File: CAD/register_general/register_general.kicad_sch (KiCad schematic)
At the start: 30 parts, among them J1 Conn_01x16_Pin, J2 Conn_01x16_Pin, U1 74HC245, U2 74HC377

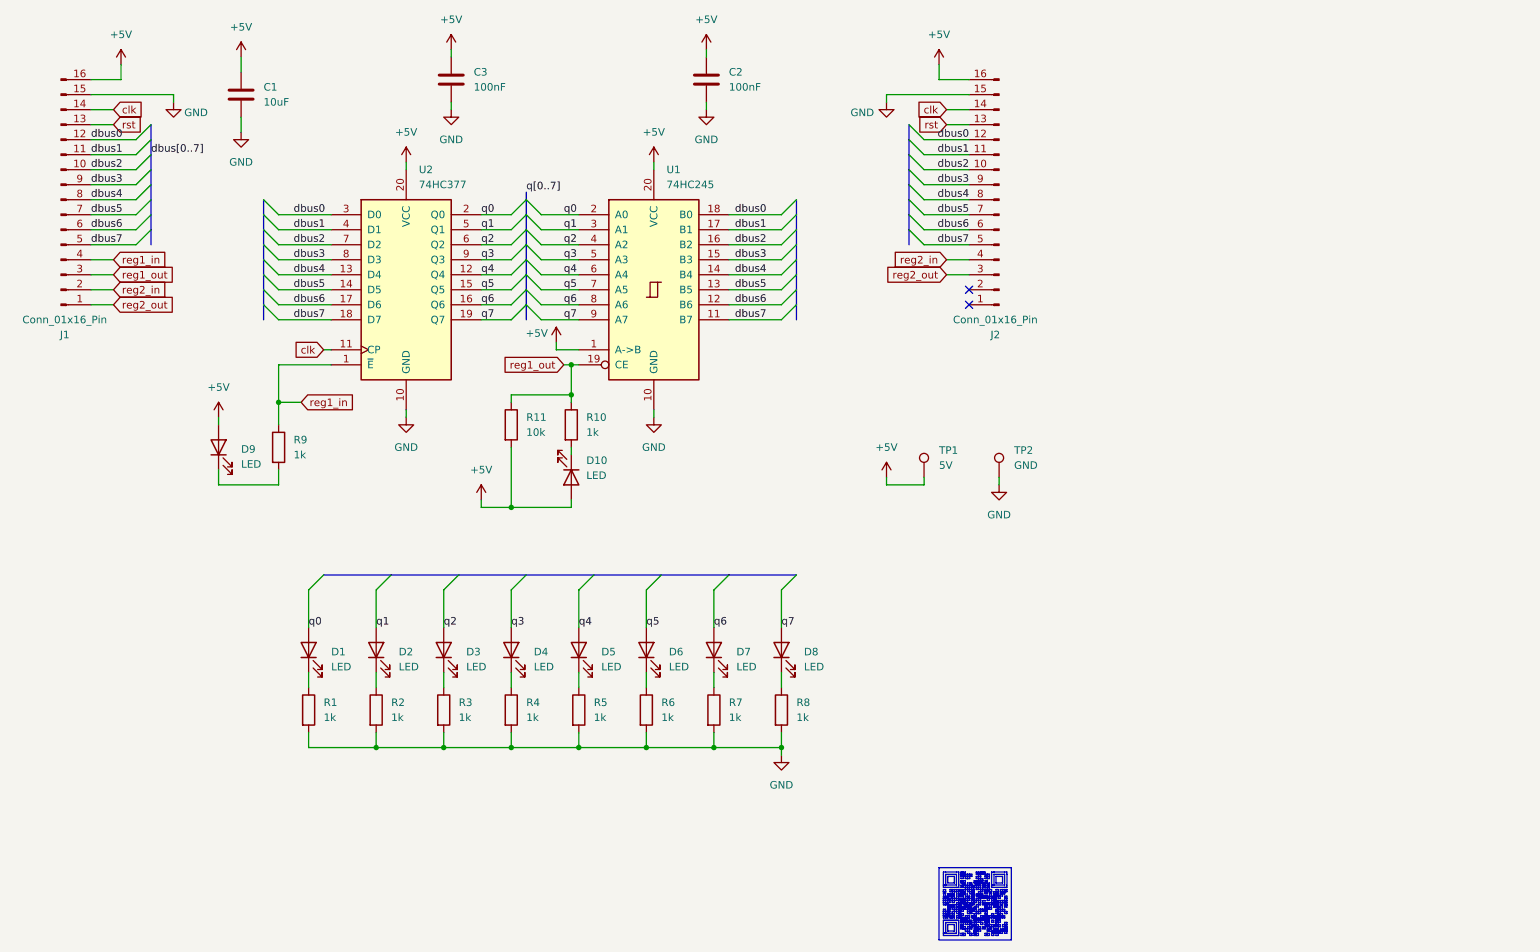
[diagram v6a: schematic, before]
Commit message: update General Register, add mounting holes, testpoints, LCSC numbers
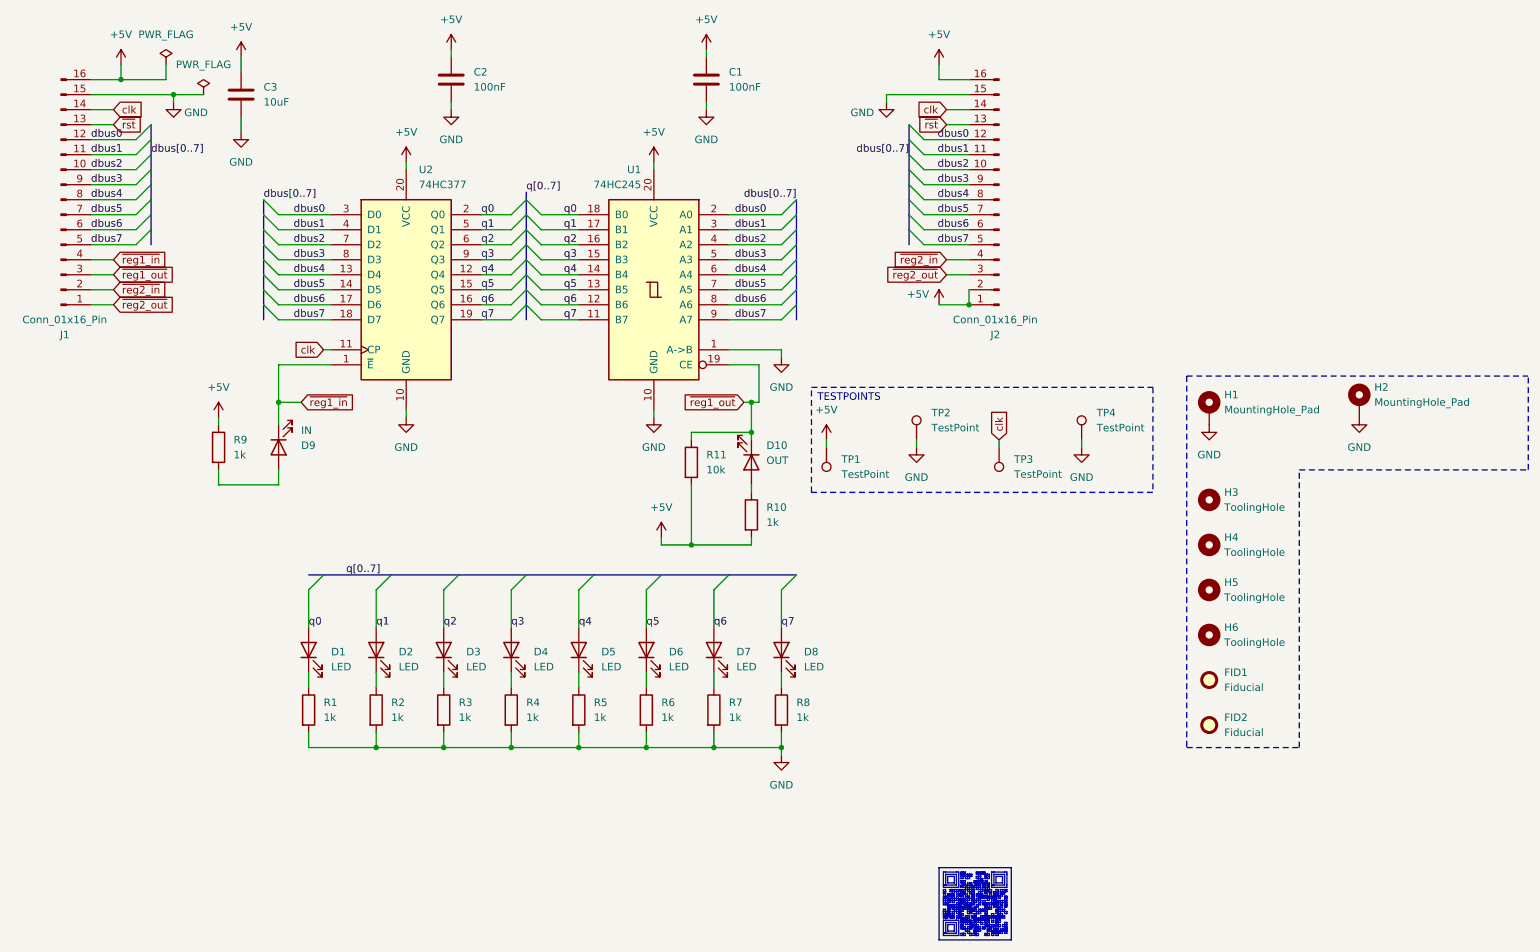
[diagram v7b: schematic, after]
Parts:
- added FID1, FID2: Fiducial, Fiducial:Fiducial_0.5mm_Mask1mm, symbol Mechanical:Fiducial
- added H1, H2: MountingHole_Pad, MountingHole:MountingHole_2.5mm_Pad_Via, symbol Mechanical:MountingHole_Pad
- added H3, H4, H5, H6: ToolingHole, MountingHole:ToolingHole_1.152mm, symbol Mechanical:MountingHole
- added TP3, TP4: TestPoint, TestPoint:TestPoint_THTPad_D1.0mm_Drill0.5mm, symbol Connector:TestPoint
- C1: renamed from C2; LCSC (none) -> C28233
- C2: renamed from C3; LCSC (none) -> C28233
- C3: renamed from C1; LCSC (none) -> C15850
- D1, D2, D3, D4, D5, D6, D7, D8: LCSC (none) -> C84256
- D10: value LED -> OUT; LCSC (none) -> C2296
- D9: value LED -> IN; LCSC (none) -> C2297
- J1: LCSC (none) -> C492436
- J2: LCSC (none) -> C22465965
- R1, R10, R2, R3, R4, R5, R6, R7, R8, R9: LCSC (none) -> C17513
- R11: LCSC (none) -> C17414
- TP1: value 5V -> TestPoint; now left out of the parts list
- TP2: value GND -> TestPoint; now left out of the parts list
- U1: footprint Package_SO:SO-20_5.3x12.6mm_P1.27mm -> Package_SO:SOIC-20W_7.5x12.8mm_P1.27mm; Details https://www.lcsc.com/product-detail/C88578.html -> https://jlcpcb.com/partdetail/Nexperia-74HC245D653/C5625; LCSC C88578 -> C5625
- U2: footprint Package_SO:SO-20_5.3x12.6mm_P1.27mm -> 8-bit_computer:SO-20_5.3x12.6mm_P1.27mm
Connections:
- net +5V: now also J2.1 (Pin_1), J2.2 (Pin_2), R10.2, R9.1; no longer D10.2 (A), D9.2 (A), U1.1 (A->B)
- net GND: now also U1.1 (A->B), H1.1, H2.1, TP4.1
- net clk: now also TP3.1
- net dbus0: now also U1.2 (A0); no longer U1.18 (B0)
- net dbus1: now also U1.3 (A1); no longer U1.17 (B1)
- net dbus2: now also U1.4 (A2); no longer U1.16 (B2)
- net dbus3: now also U1.5 (A3); no longer U1.15 (B3)
- net dbus4: now also U1.6 (A4); no longer U1.14 (B4)
- net dbus5: now also U1.7 (A5); no longer U1.13 (B5)
- net dbus6: now also U1.8 (A6); no longer U1.12 (B6)
- net dbus7: now also U1.9 (A7); no longer U1.11 (B7)
- net q0: now also U1.18 (B0); no longer U1.2 (A0)
- net q1: now also U1.17 (B1); no longer U1.3 (A1)
- net q2: now also U1.16 (B2); no longer U1.4 (A2)
- net q3: now also U1.15 (B3); no longer U1.5 (A3)
- net q4: now also U1.14 (B4); no longer U1.6 (A4)
- net q5: now also U1.13 (B5); no longer U1.7 (A5)
- net q6: now also U1.12 (B6); no longer U1.8 (A6)
- net q7: now also U1.11 (B7); no longer U1.9 (A7)
- net at R9.2: now also D9.2 (A); no longer D9.1 (K)
- net ~{reg1_out}: now reaches D10.1 (K)
- net ~{reg1_out}: now also J1.3 (Pin_3), R11.1, U1.19 (CE); no longer R10.2
- net reg1_in renamed ~{reg1_in}
- net ~{reg1_in}: now also D9.1 (K); no longer R9.1
- removed net reg1_out: J1.3 (Pin_3), R10.1, R11.1, U1.19 (CE)
- net reg2_in renamed ~{reg2_in}
- net reg2_out renamed ~{reg2_out}
- net rst renamed ~{rst}
- new net: D10.2 (A), R10.1
- no-connect marks 2 -> 0
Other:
- note added: "TESTPOINTS"
- moved on the sheet: D10, D9, R10, R11, R9

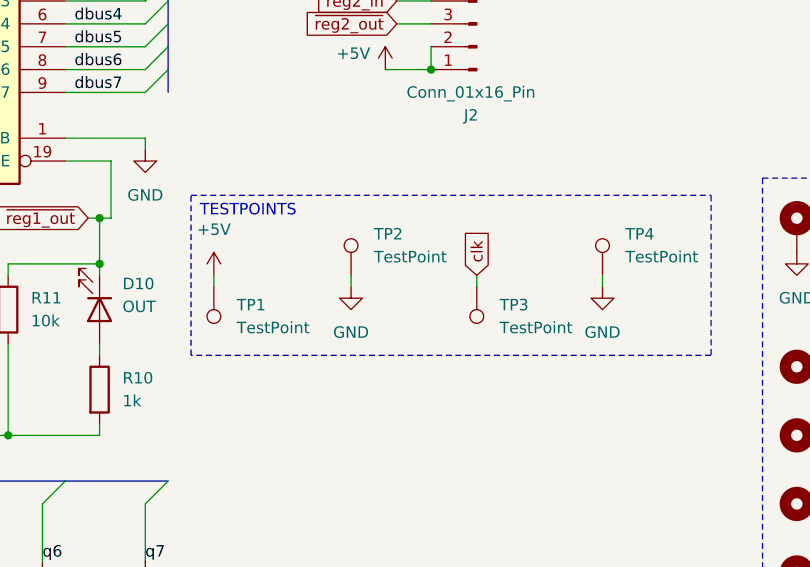
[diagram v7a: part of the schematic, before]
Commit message: add slotted test point for 5V to general register
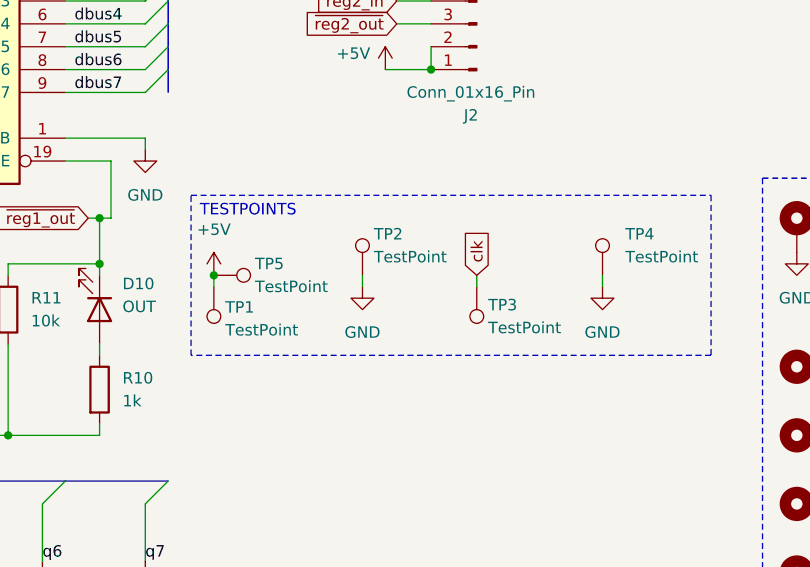
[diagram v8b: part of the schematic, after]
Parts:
- added TP5: TestPoint, 8-bit_computer:TestPoint_Slot_2.2x0.8mm, symbol Connector:TestPoint
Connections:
- net +5V: now also TP5.1
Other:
- moved on the sheet: TP2
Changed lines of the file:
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@@
 	)
 	(junction
+		(at 160.02 95.25)
+		(diameter 0)
+		(color 0 0 0 0)
+	)
+	(junction
 		(at 184.15 72.39)
 		(diameter 0)
@@
 	(wire
 		(pts
-			(xy 175.26 95.25) (xy 175.26 96.52)
+			(xy 176.53 95.25) (xy 176.53 96.52)
 		)
 		(stroke
@@
 		)
 		(instances
-			(project ""
+			(project "register_general"
 				(path "/0d96e788-3788-4603-be87-fd7748d71811"
 					(reference "#PWR03")
@@
 		)
 		(instances
-			(project ""
+			(project "register_general"
 				(path "/0d96e788-3788-4603-be87-fd7748d71811"
 					(reference "#FLG01")
@@
 	(symbol
 		(lib_id "Connector:TestPoint")
-		(at 175.26 95.25 0)
+		(at 176.53 95.25 0)
 		(unit 1)
 		(exclude_from_sim no)
@@
 		(on_board yes)
 		(dnp no)
-		(fields_autoplaced yes)
 		(property "Reference" "TP2"
-			(at 177.8 90.6779 0)
+			(at 177.8 90.678 0)
 			(effects
 				(font
@@
 		)
 		(property "Value" "TestPoint"
-			(at 177.8 93.2179 0)
+			(at 177.8 93.218 0)
 			(effects
 				(font
@@
 		)
 		(property "Footprint" "TestPoint:TestPoint_THTPad_D1.0mm_Drill0.5mm"
-			(at 180.34 95.25 0)
+			(at 181.61 95.25 0)
 			(effects
 				(font
@@
 		)
 		(property "Datasheet" "~"
-			(at 180.34 95.25 0)
+			(at 181.61 95.25 0)
 			(effects
 				(font
@@
 		)
 		(property "Description" "test point"
-			(at 175.26 95.25 0)
+			(at 176.53 95.25 0)
 			(effects
 				(font
@@
 		)
 		(instances
-			(project ""
+			(project "register_general"
 				(path "/0d96e788-3788-4603-be87-fd7748d71811"
 					(reference "#PWR09")
@@
 		)
 		(instances
-			(project ""
+			(project "register_general"
 				(path "/0d96e788-3788-4603-be87-fd7748d71811"
 					(reference "#PWR010")
@@
 		)
 		(instances
-			(project ""
+			(project "register_general"
 				(path "/0d96e788-3788-4603-be87-fd7748d71811"
 					(reference "#PWR08")
@@
 		)
 		(instances
-			(project ""
+			(project "register_general"
 				(path "/0d96e788-3788-4603-be87-fd7748d71811"
 					(reference "R11")
@@
 		)
 		(instances
-			(project ""
+			(project "register_general"
 				(path "/0d96e788-3788-4603-be87-fd7748d71811"
 					(reference "C3")
@@
 	(symbol
 		(lib_id "Connector:TestPoint")
+		(at 160.02 95.25 270)
+		(unit 1)
+		(exclude_from_sim no)
+		(in_bom no)
+		(on_board yes)
+		(dnp no)
+		(property "Reference" "TP5"
+			(at 164.592 93.98 90)
+			(effects
+				(font
+					(size 1.27 1.27)
+				)
+				(justify left)
+			)
+		)
+		(property "Value" "TestPoint"
+			(at 164.592 96.52 90)
+			(effects
+				(font
+					(size 1.27 1.27)
+				)
+				(justify left)
+			)
+		)
+		(property "Footprint" "8-bit_computer:TestPoint_Slot_2.2x0.8mm"
+			(at 160.02 100.33 0)
+			(effects
+				(font
+					(size 1.27 1.27)
+				)
+				(hide yes)
+			)
+		)
+		(property "Datasheet" "~"
+			(at 160.02 100.33 0)
+			(effects
+				(font
+					(size 1.27 1.27)
+				)
+				(hide yes)
+			)
+		)
+		(property "Description" "Oval slot probe hook plated"
+			(at 160.02 95.25 0)
+			(effects
+				(font
+					(size 1.27 1.27)
+				)
+				(hide yes)
+			)
+		)
+		(pin "1"
+		)
+		(instances
+			(project "register_general"
+				(path "/0d96e788-3788-4603-be87-fd7748d71811"
+					(reference "TP5")
+					(unit 1)
+				)
+			)
+		)
+	)
+	(symbol
+		(lib_id "Connector:TestPoint")
 		(at 160.02 96.52 180)
 		(unit 1)
@@
 		(on_board yes)
 		(dnp no)
-		(fields_autoplaced yes)
 		(property "Reference" "TP1"
-			(at 162.56 98.5519 0)
+			(at 161.29 98.806 0)
 			(effects
 				(font
@@
 		)
 		(property "Value" "TestPoint"
-			(at 162.56 101.0919 0)
+			(at 161.29 101.346 0)
 			(effects
 				(font
@@
 		)
 		(instances
-			(project ""
+			(project "register_general"
 				(path "/0d96e788-3788-4603-be87-fd7748d71811"
 					(reference "U2")
@@
 	(symbol
 		(lib_id "power:GND")
-		(at 175.26 96.52 0)
+		(at 176.53 96.52 0)
 		(unit 1)
 		(exclude_from_sim no)
@@
 		(on_board yes)
 		(dnp no)
-		(fields_autoplaced yes)
 		(property "Reference" "#PWR031"
-			(at 175.26 102.87 0)
+			(at 176.53 102.87 0)
 			(effects
 				(font
@@
 		)
 		(property "Value" "GND"
-			(at 175.26 101.6 0)
+			(at 176.53 101.6 0)
 			(effects
 				(font
@@
 		)
 		(property "Footprint" ""
-			(at 175.26 96.52 0)
+			(at 176.53 96.52 0)
 			(effects
 				(font
@@
 		)
 		(property "Datasheet" ""
-			(at 175.26 96.52 0)
+			(at 176.53 96.52 0)
 			(effects
 				(font
@@
 		)
 		(property "Description" "Power symbol creates a global label with name \"GND\" , ground"
-			(at 175.26 96.52 0)
+			(at 176.53 96.52 0)
 			(effects
 				(font
@@
 		)
 		(instances
-			(project ""
+			(project "register_general"
 				(path "/0d96e788-3788-4603-be87-fd7748d71811"
 					(reference "U1")
@@
 		)
 		(instances
-			(project ""
+			(project "register_general"
 				(path "/0d96e788-3788-4603-be87-fd7748d71811"
 					(reference "C1")
@@
 		(on_board yes)
 		(dnp no)
-		(fields_autoplaced yes)
 		(property "Reference" "TP3"
-			(at 191.77 98.5519 0)
+			(at 190.5 98.552 0)
 			(effects
 				(font
@@
 		)
 		(property "Value" "TestPoint"
-			(at 191.77 101.0919 0)
+			(at 190.5 101.092 0)
 			(effects
 				(font
@@
 		)
 		(instances
-			(project ""
+			(project "register_general"
 				(path "/0d96e788-3788-4603-be87-fd7748d71811"
 					(reference "#PWR01")
